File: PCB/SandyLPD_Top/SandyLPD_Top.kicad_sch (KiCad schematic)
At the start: 11 parts

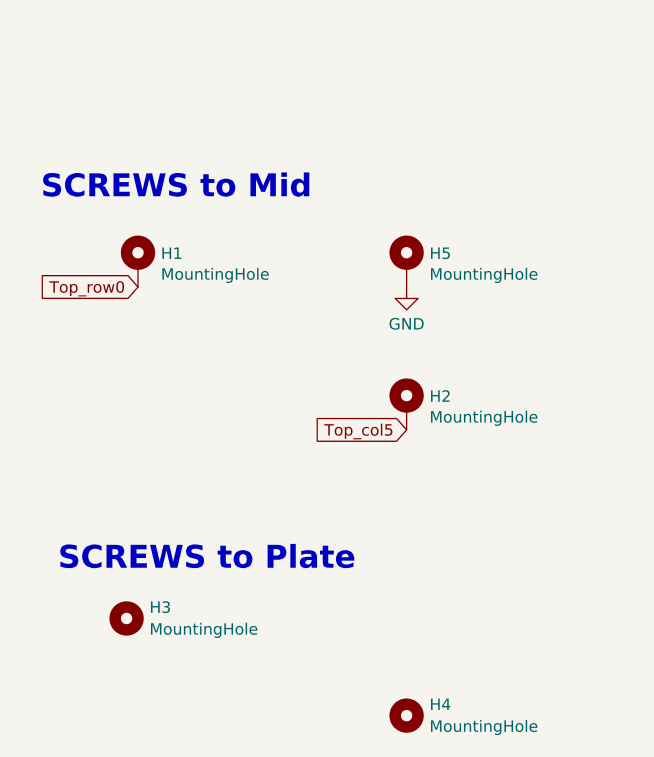
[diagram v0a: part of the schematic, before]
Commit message: ネジの3Dモデル追加
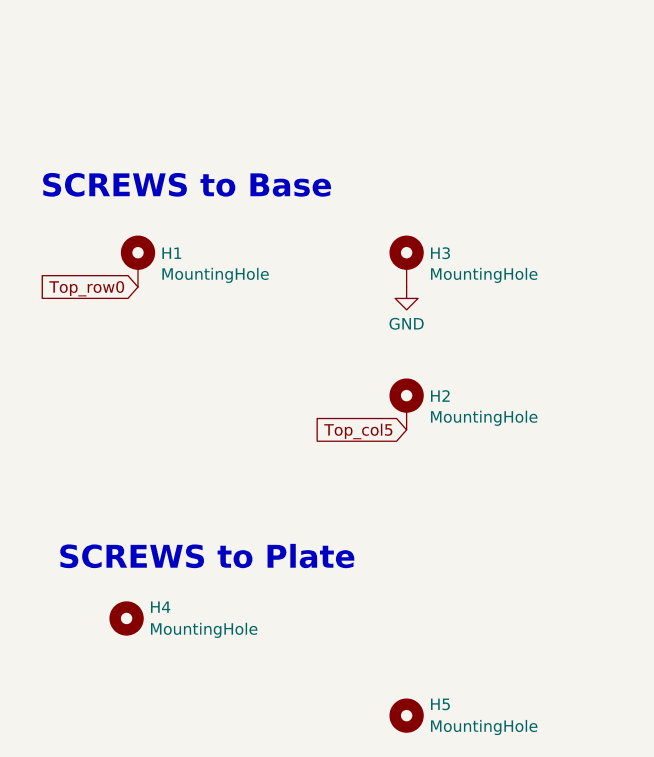
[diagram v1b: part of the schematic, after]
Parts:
- H1, H2: footprint locallib:MountingHole_2.2mm_M2_Pad_minimal -> locallib:MountingHole_2.2mm_M2_Pad_minimal_L8mm_SlimHead
- H3: renamed from H5; footprint locallib:MountingHole_2.2mm_M2_Pad_minimal -> locallib:MountingHole_2.2mm_M2_Pad_minimal_L8mm_SlimHead
- renumbered H3 to H4, H4 to H5
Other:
- note added: "SCREWS to Base"
- note removed: "SCREWS to Mid"
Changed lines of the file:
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@@
 		)
 	)
-	(text "SCREWS to Mid"
+	(text "SCREWS to Base"
 		(exclude_from_sim no)
 		(at 28.575 110.49 0)
@@
 			)
 		)
-		(property "Footprint" "locallib:MountingHole_2.2mm_M2_Pad_minimal"
+		(property "Footprint" "locallib:MountingHole_2.2mm_M2_Pad_minimal_L8mm_SlimHead"
 			(at 39.37 117.475 0)
 			(effects
@@
 			)
 		)
-		(property "Footprint" "locallib:MountingHole_2.2mm_M2_Pad_minimal"
+		(property "Footprint" "locallib:MountingHole_2.2mm_M2_Pad_minimal_L8mm_SlimHead"
 			(at 69.215 133.35 0)
 			(effects
@@
 		(dnp no)
 		(fields_autoplaced yes)
-		(property "Reference" "H3"
+		(property "Reference" "H4"
 			(at 40.64 155.6328 0)
 			(effects
@@
 			(project "SandyLPD_Top"
 				(path "/a99ab643-cdc7-4f8c-8088-c1f4faa914d1"
-					(reference "H3")
+					(reference "H4")
 					(unit 1)
 				)
@@
 		(dnp no)
 		(fields_autoplaced yes)
-		(property "Reference" "H4"
+		(property "Reference" "H5"
 			(at 71.755 166.4278 0)
 			(effects
@@
 			(project "SandyLPD_Top"
 				(path "/a99ab643-cdc7-4f8c-8088-c1f4faa914d1"
-					(reference "H4")
+					(reference "H5")
 					(unit 1)
 				)
@@
 		(on_board yes)
 		(dnp no)
-		(property "Reference" "H5"
+		(property "Reference" "H3"
 			(at 71.755 116.3066 0)
 			(effects
@@
 			)
 		)
-		(property "Footprint" "locallib:MountingHole_2.2mm_M2_Pad_minimal"
+		(property "Footprint" "locallib:MountingHole_2.2mm_M2_Pad_minimal_L8mm_SlimHead"
 			(at 69.215 117.475 0)
 			(effects
@@
 			(project "Sandy_Top_with_Plate_Mid"
 				(path "/a99ab643-cdc7-4f8c-8088-c1f4faa914d1"
-					(reference "H5")
-					(unit 1)
-				)
+					(reference "H3")
+					(unit 1)
+				)

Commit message: ネジ等の3Dモデル追加
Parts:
- H1, H2, H3: footprint locallib:MountingHole_2.2mm_M2_Pad_minimal_L8mm_SlimHead -> locallib:MountingHole_2.2mm_M2_Pad_minimal_L8mm_SlimHead_L3.5mm_Spacer_Backside
- H4, H5: footprint locallib:MountingHole_M2_Through-hole_tap_THC-0.8-x-2 -> locallib:MountingHole_M2_Through-hole_tap_THC-0.8-1.0-2
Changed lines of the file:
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@@
 			)
 		)
-		(property "Footprint" "locallib:MountingHole_2.2mm_M2_Pad_minimal_L8mm_SlimHead"
+		(property "Footprint" "locallib:MountingHole_2.2mm_M2_Pad_minimal_L8mm_SlimHead_L3.5mm_Spacer_Backside"
 			(at 39.37 117.475 0)
 			(effects
@@
 			)
 		)
-		(property "Footprint" "locallib:MountingHole_2.2mm_M2_Pad_minimal_L8mm_SlimHead"
+		(property "Footprint" "locallib:MountingHole_2.2mm_M2_Pad_minimal_L8mm_SlimHead_L3.5mm_Spacer_Backside"
 			(at 69.215 133.35 0)
 			(effects
@@
 			)
 		)
-		(property "Footprint" "locallib:MountingHole_M2_Through-hole_tap_THC-0.8-x-2"
+		(property "Footprint" "locallib:MountingHole_M2_Through-hole_tap_THC-0.8-1.0-2"
 			(at 38.1 156.845 0)
 			(effects
@@
 			)
 		)
-		(property "Footprint" "locallib:MountingHole_M2_Through-hole_tap_THC-0.8-x-2"
+		(property "Footprint" "locallib:MountingHole_M2_Through-hole_tap_THC-0.8-1.0-2"
 			(at 69.215 167.64 0)
 			(effects
@@
 			)
 		)
-		(property "Footprint" "locallib:MountingHole_2.2mm_M2_Pad_minimal_L8mm_SlimHead"
+		(property "Footprint" "locallib:MountingHole_2.2mm_M2_Pad_minimal_L8mm_SlimHead_L3.5mm_Spacer_Backside"
 			(at 69.215 117.475 0)
 			(effects
